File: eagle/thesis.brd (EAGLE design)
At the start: 99.1 x 60.2 mm, 18 parts, among them J1 RJ11-6PTH, U1 ITG-3200, U2 ADXL362

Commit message: wrote a bunch and added references and pictures
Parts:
- renumbered J1 to JHMR2300, U$4 to HMC5883L
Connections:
- net 33V: now also C6.2
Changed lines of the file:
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@@
 <attribute name="PROD_ID" value="IC-11297" x="92.964" y="5.842" size="1.778" layer="27" display="off"/>
 </element>
-<element name="J1" library="SparkFun-Connectors" package="RJ11-6" value="RJ11-6PTH" x="12.319" y="51.181" rot="R180"/>
-<element name="U$4" library="HMC5883L_Breakout-v11" package="SPARKFUN_16LPCC" value="SPARKFUN_HMC5883LSMD" x="60.071" y="43.815" smashed="yes" rot="R90">
+<element name="JHMR2300" library="SparkFun-Connectors" package="RJ11-6" value="RJ11-6PTH" x="12.319" y="51.181" rot="R180"/>
+<element name="HMC5883L" library="HMC5883L_Breakout-v11" package="SPARKFUN_16LPCC" value="SPARKFUN_HMC5883LSMD" x="60.071" y="43.815" smashed="yes" rot="R90">
 <attribute name="VALUE" x="62.611" y="41.91" size="0.6096" layer="27" rot="R90"/>
 </element>
@@
 <signal name="N$5">
 <contactref element="C5" pad="1"/>
-<contactref element="U$4" pad="8"/>
+<contactref element="HMC5883L" pad="8"/>
 <wire x1="62.992" y1="44.577" x2="61.468" y2="44.577" width="0.254" layer="1"/>
 <wire x1="62.992" y1="46.736" x2="62.992" y2="44.577" width="0.254" layer="1"/>
@@
 </signal>
 <signal name="N$7">
-<contactref element="U$4" pad="12"/>
+<contactref element="HMC5883L" pad="12"/>
 <contactref element="C5" pad="2"/>
 <wire x1="58.166" y1="46.355" x2="59.309" y2="45.212" width="0.254" layer="1"/>
@@
 </signal>
 <signal name="N$12">
-<contactref element="U$4" pad="10"/>
+<contactref element="HMC5883L" pad="10"/>
 <contactref element="C3" pad="1"/>
 <wire x1="60.325" y1="44.069" x2="60.325" y2="45.085" width="0.254" layer="1"/>
@@
 <contactref element="U2" pad="P$14"/>
 <contactref element="U$1" pad="3V3"/>
-<contactref element="U$4" pad="2"/>
-<contactref element="U$4" pad="4"/>
-<contactref element="U$4" pad="13"/>
-<contactref element="R2" pad="2"/>
-<contactref element="R1" pad="2"/>
 <contactref element="C4" pad="1"/>
 <contactref element="U1" pad="9"/>
-<contactref element="J1" pad="2"/>
+<contactref element="JHMR2300" pad="2"/>
 <wire x1="41.402" y1="45.466" x2="41.402" y2="45.085" width="0.254" layer="1"/>
 <wire x1="41.402" y1="45.085" x2="41.307" y2="45.081" width="0.254" layer="1"/>
@@
 <wire x1="40.513" y1="46.99" x2="40.513" y2="45.593" width="0.254" layer="1"/>
 <wire x1="41.148" y1="47.625" x2="40.513" y2="46.99" width="0.254" layer="1"/>
-<wire x1="57.023" y1="46.228" x2="58.3565" y2="44.8945" width="0.254" layer="1"/>
-<wire x1="58.3565" y1="44.8945" x2="58.674" y2="44.577" width="0.254" layer="1"/>
-<wire x1="57.023" y1="46.482" x2="57.023" y2="46.228" width="0.254" layer="1"/>
-<wire x1="56.134" y1="47.371" x2="57.023" y2="46.482" width="0.254" layer="1"/>
-<wire x1="58.674" y1="44.577" x2="58.701" y2="44.565" width="0.254" layer="1"/>
-<wire x1="56.134" y1="47.371" x2="56.134" y2="47.459" width="0.254" layer="1"/>
-<wire x1="59.817" y1="41.148" x2="59.817" y2="42.418" width="0.254" layer="1"/>
-<wire x1="60.706" y1="39.624" x2="59.817" y2="41.148" width="0.254" layer="1"/>
-<wire x1="59.817" y1="42.418" x2="59.821" y2="42.445" width="0.254" layer="1"/>
-<wire x1="60.706" y1="39.624" x2="60.794" y2="39.624" width="0.254" layer="1"/>
 <wire x1="60.833" y1="39.624" x2="60.833" y2="41.275" width="0.254" layer="1"/>
 <wire x1="60.833" y1="41.275" x2="60.833" y2="42.418" width="0.254" layer="1"/>
-<wire x1="60.833" y1="42.418" x2="60.821" y2="42.445" width="0.254" layer="1"/>
-<wire x1="60.833" y1="39.624" x2="60.794" y2="39.624" width="0.254" layer="1"/>
 <wire x1="60.833" y1="41.275" x2="63.881" y2="44.323" width="0.254" layer="1"/>
 <wire x1="63.881" y1="44.323" x2="63.881" y2="44.436" width="0.254" layer="1"/>
@@
 <wire x1="63.881" y1="44.436" x2="63.881" y2="44.958" width="0.254" layer="1"/>
 <wire x1="78.105" y1="49.784" x2="78.105" y2="49.856" width="0.254" layer="1"/>
-<wire x1="56.388" y1="43.18" x2="58.3565" y2="44.8945" width="0.254" layer="1"/>
-<wire x1="56.388" y1="41.148" x2="56.388" y2="43.18" width="0.254" layer="1"/>
-<wire x1="59.817" y1="41.148" x2="56.388" y2="41.148" width="0.254" layer="1"/>
 <wire x1="60.452" y1="45.466" x2="41.148" y2="45.466" width="0.254" layer="16"/>
 <wire x1="61.341" y1="46.355" x2="60.452" y2="45.466" width="0.254" layer="16"/>
@@
 <contactref element="C7" pad="2"/>
 <contactref element="U1" pad="13"/>
-<wire x1="42.037" y1="48.895" x2="42.051" y2="48.895" width="0" layer="19" extent="1-1"/>
+<contactref element="R2" pad="2"/>
+<contactref element="R1" pad="2"/>
+<wire x1="57.023" y1="46.228" x2="58.3565" y2="44.8945" width="0.254" layer="1"/>
+<wire x1="58.3565" y1="44.8945" x2="58.674" y2="44.577" width="0.254" layer="1"/>
+<wire x1="57.023" y1="46.482" x2="57.023" y2="46.228" width="0.254" layer="1"/>
+<wire x1="56.134" y1="47.371" x2="57.023" y2="46.482" width="0.254" layer="1"/>
+<wire x1="59.817" y1="41.148" x2="59.817" y2="42.418" width="0.254" layer="1"/>
+<wire x1="60.706" y1="39.624" x2="59.817" y2="41.148" width="0.254" layer="1"/>
+<wire x1="60.706" y1="39.624" x2="60.794" y2="39.624" width="0.254" layer="1"/>
+<wire x1="56.388" y1="43.18" x2="58.3565" y2="44.8945" width="0.254" layer="1"/>
+<wire x1="56.388" y1="41.148" x2="56.388" y2="43.18" width="0.254" layer="1"/>
+<wire x1="59.817" y1="41.148" x2="56.388" y2="41.148" width="0.254" layer="1"/>
+<contactref element="HMC5883L" pad="2"/>
+<contactref element="HMC5883L" pad="4"/>
+<contactref element="HMC5883L" pad="13"/>
+<contactref element="C6" pad="2"/>
+<wire x1="56.134" y1="47.371" x2="56.134" y2="47.459" width="0" layer="19" extent="1-1"/>
+<wire x1="58.701" y1="44.565" x2="58.674" y2="44.577" width="0" layer="19" extent="1-1"/>
+<wire x1="59.821" y1="42.445" x2="59.817" y2="42.418" width="0" layer="19" extent="1-1"/>
+<wire x1="60.833" y1="39.624" x2="60.794" y2="39.624" width="0" layer="19" extent="1-1"/>
+<wire x1="42.051" y1="48.895" x2="42.037" y2="48.895" width="0" layer="19" extent="1-1"/>
+<wire x1="60.821" y1="42.445" x2="60.833" y2="42.418" width="0" layer="19" extent="1-1"/>
 <wire x1="41.307" y1="45.581" x2="41.275" y2="45.593" width="0" layer="19" extent="1-1"/>
 <wire x1="42.057" y1="42.831" x2="42.037" y2="42.799" width="0" layer="19" extent="1-1"/>
 <wire x1="41.402" y1="45.466" x2="41.307" y2="45.581" width="0" layer="19" extent="1-1"/>
+<wire x1="42.559" y1="40.259" x2="42.037" y2="42.799" width="0" layer="19" extent="1-1"/>
 </signal>
 <signal name="5V">
@@
 <signal name="VIN">
 <contactref element="U$1" pad="VIN"/>
-<contactref element="J1" pad="5"/>
+<contactref element="JHMR2300" pad="5"/>
 <wire x1="40.259" y1="8.255" x2="42.926" y2="5.588" width="0.254" layer="16"/>
 <wire x1="19.558" y1="8.255" x2="40.259" y2="8.255" width="0.254" layer="16"/>
@@
 </signal>
 <signal name="TX1">
-<contactref element="J1" pad="4"/>
+<contactref element="JHMR2300" pad="4"/>
 <contactref element="U$1" pad="TX1"/>
 <wire x1="74.041" y1="55.753" x2="75.946" y2="53.848" width="0.254" layer="16"/>
@@
 </signal>
 <signal name="RX1">
-<contactref element="J1" pad="3"/>
+<contactref element="JHMR2300" pad="3"/>
 <contactref element="U$1" pad="RX1"/>
 <wire x1="75.184" y1="50.546" x2="78.486" y2="53.848" width="0.254" layer="16"/>
@@
 <signal name="SCL">
 <contactref element="U$3" pad="7"/>
-<contactref element="U$4" pad="1"/>
+<contactref element="HMC5883L" pad="1"/>
 <contactref element="R2" pad="1"/>
 <contactref element="U$1" pad="SCL"/>
@@
 </signal>
 <signal name="SDA" airwireshidden="yes">
-<contactref element="U$4" pad="16"/>
+<contactref element="HMC5883L" pad="16"/>
 <contactref element="R1" pad="1"/>
 <contactref element="U$1" pad="SDA"/>
@@
 <signal name="GND1_1">
 <contactref element="U$1" pad="GND1"/>
-<contactref element="J1" pad="1"/>
+<contactref element="JHMR2300" pad="1"/>
 <contactref element="U$6" pad="GND"/>
 <contactref element="U$2" pad="6"/>
@@
 <contactref element="C3" pad="2"/>
 <contactref element="C4" pad="2"/>
-<contactref element="U$4" pad="9"/>
-<contactref element="U$4" pad="11"/>
+<contactref element="HMC5883L" pad="9"/>
+<contactref element="HMC5883L" pad="11"/>
 <wire x1="44.577" y1="40.513" x2="44.577" y2="41.783" width="0.254" layer="1"/>
 <wire x1="44.577" y1="41.783" x2="44.577" y2="42.799" width="0.254" layer="1"/>

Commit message: wrote more.
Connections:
- new net SCL1: U$1.SCL1, U1.23
- new net SDA1: U$1.SDA1, U1.24
- net 33V: now also JHMR2300.5; no longer JHMR2300.2
- net GND1_1: now also JHMR2300.6; no longer JHMR2300.1
- net RX1: now also JHMR2300.4; no longer JHMR2300.3
- net SCL: no longer U1.23
- net SDA: no longer U1.24
- net TX1: now also JHMR2300.3; no longer JHMR2300.4
- net VIN: now also JHMR2300.2; no longer JHMR2300.5
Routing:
- net SCL1: track 0.00 -> 41.9 mm
- net SDA1: track 0.00 -> 36.0 mm
- net D48: track 123.3 -> 102.7 mm, vias 0 -> 1
- net SDA: track 88.6 -> 104.8 mm
- net D47: track 103.1 -> 117.7 mm, vias 2 -> 1
- net RX3: track 87.1 -> 100.8 mm
- net TX3: track 76.0 -> 88.9 mm
- net SCLK: track 128.9 -> 117.7 mm
- net RX1: track 77.3 -> 87.5 mm
- net D38: track 79.5 -> 71.3 mm
- net D41: track 79.4 -> 71.5 mm, vias 0 -> 1
- net GNDHEAD: track 97.5 -> 90.0 mm, vias 0 -> 3
- net 5V: track 52.9 -> 59.4 mm
- net D49: track 100.5 -> 105.3 mm, vias 2 -> 0
- net 33V: track 232.8 -> 237.1 mm
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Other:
- board text added: "ADAM CHASE 09/10/13 FDR v2.10"
- board text removed: "ADAM CHASE 08/13/13 FDR v2.00"

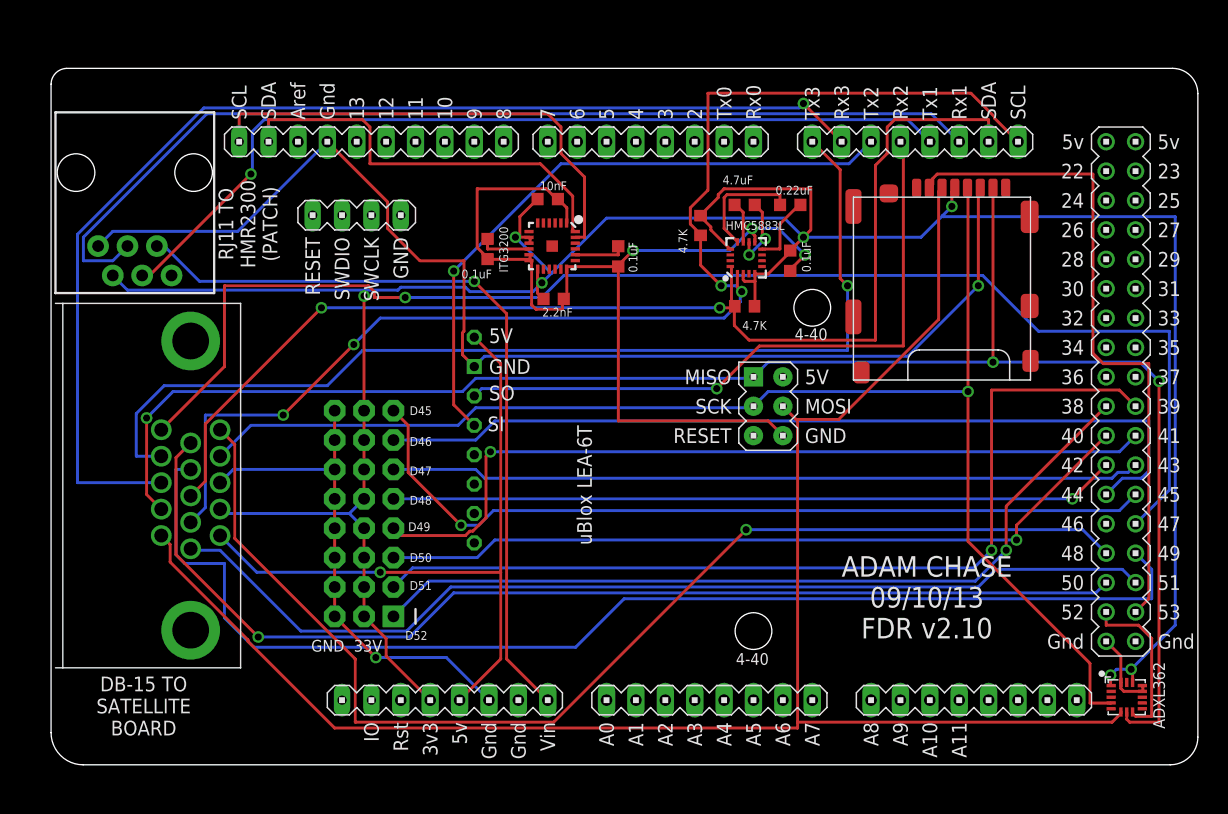
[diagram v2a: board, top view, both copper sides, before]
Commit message: added breakout board libraries and changed thesis.brd
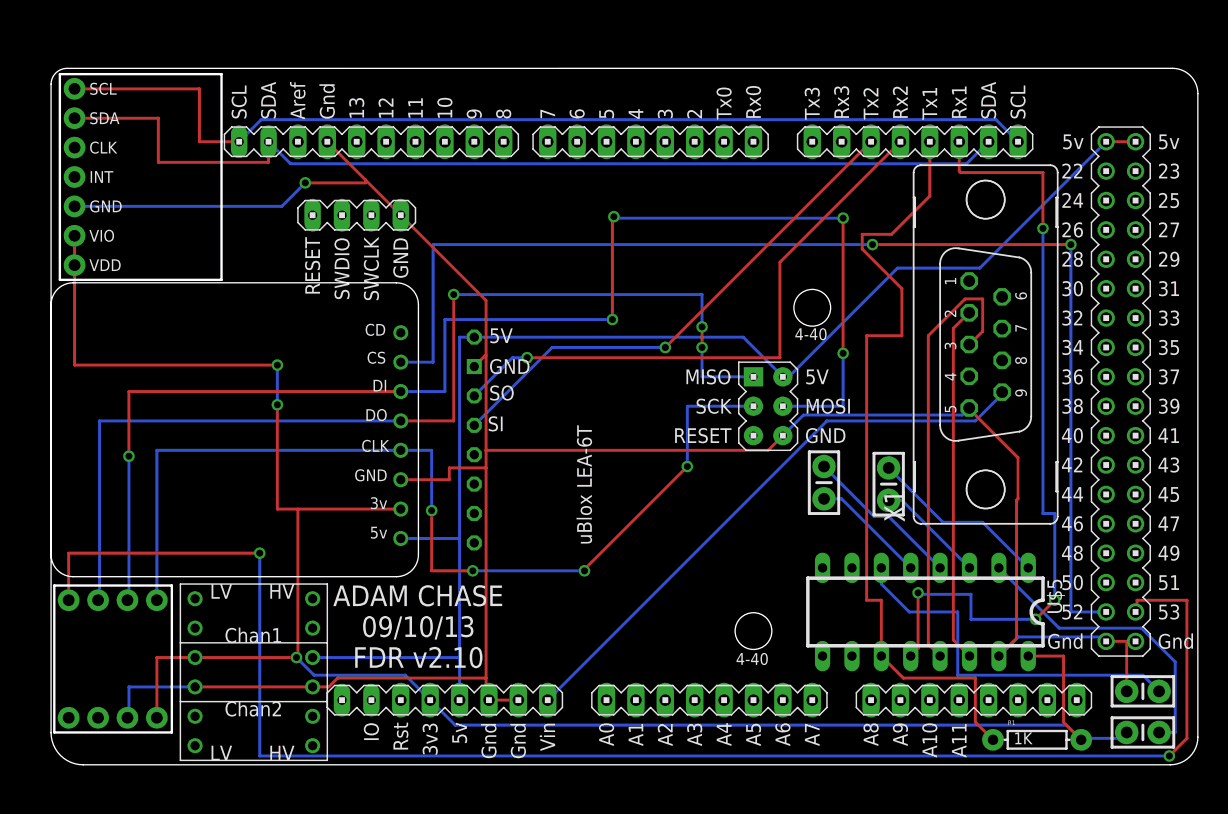
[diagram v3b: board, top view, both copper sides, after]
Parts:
- removed C5: 0.22uF, rcl:C0603K
- removed C6: 0.1uF, rcl:C0603K
- removed C7: 10nF, rcl:C0603K
- removed HMC5883L: SPARKFUN_HMC5883LSMD, HMC5883L_Breakout-v11:SPARKFUN_16LPCC
- removed JHMR2300: RJ11-6PTH, SparkFun-Connectors:RJ11-6
- removed R2: 4.7K, rcl:R0603
- removed U1: ITG-3200, SparkFun:QFN-24
- removed U2: ADXL362, SparkFun-Sensors:ADXL362
- added U$4: ADXL362, adxl362:ADXL362
- added U$7: ITG3200, ITG3200:ITG3200
- added X1: (no value), con-subd:F09V
- C1, C4: value 0.1uF -> 100nF; device rcl:C0603K -> SparkFun-Passives:CAP-PTH-SMALL-KIT
- C2: value 2.2nF -> 100nF; device rcl:C0603K -> SparkFun-Passives:CAP-PTH-SMALL-KIT
- C3: value 4.7uF -> 100nF; device rcl:C0603K -> SparkFun-Passives:CAP-PTH-SMALL-KIT
- R1: value 4.7K -> 1K; device rcl:R0603 -> SparkFun-Resistors:AXIAL-0.3
- U$2: value MICROSD_SPI_MODE -> LOGIC_LEVEL_CONVERTER; device con-molex-microsd:MICRO_SD_CONNECTOR -> SparkFun-Boards:LOGIC_LEVEL_CONVERTER
- U$3: value VGA-F90S -> MICROSD; device VideoConnectors:DB-15-F90+SHIELD-SMALL_PADS -> MICROSD:MICROSD
- U$5: value HEADER-3X8SERVO -> ICL3232; device pixhawk2:3X8RA -> SparkFun-DigitalIC:DIL16
- moved U$2 77.6 mm to (11.2, 0.38)
- moved C3 54.3 mm to (94.4, 6.35)
- moved C4 50.9 mm to (94.4, 2.79), turned to 0 degrees
- moved U$5 48.0 mm to (75.6, 13.2)
- moved R1 45.2 mm to (85.2, 2.16)
- moved C1 40.2 mm to (72.4, 24.3), turned to 270 degrees
- moved C2 26.4 mm to (66.8, 24.4), turned to 270 degrees
- moved U$3 8.41 mm to (-0.25, 15.7), turned to 0 degrees
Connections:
- removed net 33V: C4.1, C6.2, C7.2, HMC5883L.13, HMC5883L.2, HMC5883L.4, JHMR2300.5, R1.2, R2.2, U$1.3V3, U$2.4, U$3.2, U$5.11, U$5.14, U$5.17, U$5.2, U$5.20, U$5.23, U$5.5, U$5.8, U1.13, U1.8, U1.9, U2.P$1, U2.P$14
- removed net CPOUT: C2.2, U1.20
- removed net D52: U$1.52, U2.P$8
- removed net D53: U$1.53, U$2.2
- removed net GND1: U$1.GND_1, U$3.3, U$5.12, U$5.15, U$5.18, U$5.21, U$5.24, U$5.3, U$5.6, U$5.9
- removed net GND1_1: JHMR2300.6, U$1.GND1, U$2.6, U$6.GND
- removed net GND2: U$1.GND_2
- removed net GNDA: U$1.GND_A, U2.P$12, U2.P$13, U2.P$16
- removed net GNDHEAD: C1.1, C2.1, C3.2, C4.2, C6.1, C7.1, HMC5883L.11, HMC5883L.9, U$1.5V_ICSP, U1.1, U1.11, U1.12, U1.18
- removed net N$12: C3.1, HMC5883L.10
- removed net N$14: C1.2, U1.10
- removed net N$5: C5.1, HMC5883L.8
- removed net N$7: C5.2, HMC5883L.12
- removed net RX1: JHMR2300.4, U$1.RX1
- removed net SCL1: U$1.SCL1, U1.23
- removed net SDA: HMC5883L.16, R1.1, U$1.SDA, U$3.8
- removed net SDA1: U$1.SDA1, U1.24
- removed net TX1: JHMR2300.3, U$1.TX1
- new net 3V3: C4.1, R1.P$2, U$1.3V3, U$2.P$3, U$3.3V, U$4.VCC, U$5.16, U$7.VDD, U$7.VIO
- new net ACCELCS: U$1.53, U$4.CS
- new net C1+: C1.1, U$5.1
- new net C1-: C1.2, U$5.3
- new net C2+: C2.1, U$5.4
- new net C2-: C2.2, U$5.5
- new net GND: C3.2, U$1.5V_ICSP, U$1.GND1, U$1.GND_1, U$1.GND_2, U$1.GND_A, U$1.GND_B, U$1.GND_DEBUG, U$2.P$4, U$2.P$9, U$3.GND, U$4.GND, U$5.15, U$6.GND, U$7.GND, X1.5
- new net MAGSI: R1.P$1, U$1.TX1, U$5.11
- new net MAGSO: U$1.RX1, U$5.12
- new net RS232SI: U$5.13, X1.3
- new net RS232SO: U$5.14, X1.2
- new net SDA2: U$1.SDA, U$1.SDA1, U$7.SDA
- new net SDCS: U$1.52, U$3.CS
- new net V+: C4.2, U$5.2
- new net V-: C3.1, U$5.6
- net 5V: now also U$1.5V_A, U$1.5V_B, U$1.GND_ICSP, U$2.P$10, U$3.5V; no longer U$3.1
- net D38: no longer U$5.1
- net D39: no longer U$5.4
- net D40: no longer U$5.7
- net D41: no longer U$5.10
- net D42: no longer U$5.13
- net D43: no longer U$5.16
- net D44: no longer U$5.19
- net D45: no longer U$5.22
- net D47: no longer U$3.15
- net D48: no longer U$3.5
- net D49: no longer U$3.9
- net D50: no longer U$3.10
- net D51: no longer U$3.6
- net MISO: now also U$3.DO, U$4.MISO; no longer U$2.7, U$3.12, U2.P$7
- net MOSI: now also U$3.DI, U$4.MOSI; no longer U$2.3, U$3.11, U2.P$6
- net RX3: no longer U$3.13
- net SCL: now also U$1.SCL1, U$7.SCL; no longer HMC5883L.1, R2.1, U$3.7
- net SCLK: now also U$3.CLK, U$4.SCK; no longer U$2.5, U$3.4, U2.P$4
- net TX3: no longer U$3.14
- net VIN: now also X1.9; no longer JHMR2300.2
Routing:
- net 33V: track 237.1 -> 0.00 mm, vias 7 -> 0
- net GND: track 0.00 -> 210.7 mm, vias 0 -> 1
- net 3V3: track 0.00 -> 168.0 mm, vias 0 -> 3
- net ACCELCS: track 0.00 -> 136.3 mm, vias 0 -> 2
- net D47: track 117.7 -> 0.00 mm, vias 1 -> 0
- net GND1_1: track 105.5 -> 0.00 mm, vias 1 -> 0
- net D49: track 105.3 -> 0.00 mm
- net SDA: track 104.8 -> 0.00 mm, vias 2 -> 0
- net SDCS: track 0.00 -> 102.9 mm, vias 0 -> 2
- net D48: track 102.7 -> 0.00 mm, vias 1 -> 0
- net RX3: track 100.8 -> 0.00 mm, vias 1 -> 0
- net D50: track 95.5 -> 0.00 mm, vias 1 -> 0
- net GNDHEAD: track 90.0 -> 0.00 mm, vias 3 -> 0
- net TX3: track 88.9 -> 0.00 mm, vias 1 -> 0
- net RX1: track 87.5 -> 0.00 mm
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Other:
- board text removed: "0.1uF"
- board text removed: "0.22uF"
- board text removed: "10nF"
- board text removed: "2.2nF"
- board text removed: "33V"
- board text removed: "4.7K"
- board text removed: "4.7uF"
- board text removed: "ADXL362"
- board text removed: "D45"
- board text removed: "D46"
- board text removed: "D47"
- board text removed: "D48"
- board text removed: "D49"
- board text removed: "D50"
- board text removed: "D51"
- board text removed: "D52"
- board text removed: "DB-15 TO SATELLITE BOARD"
- board text removed: "HMC5883L"
- board text removed: "ITG3200"
- board text removed: "RJ11 TO HMR2300 (PATCH)"

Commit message: added smaller satellite board
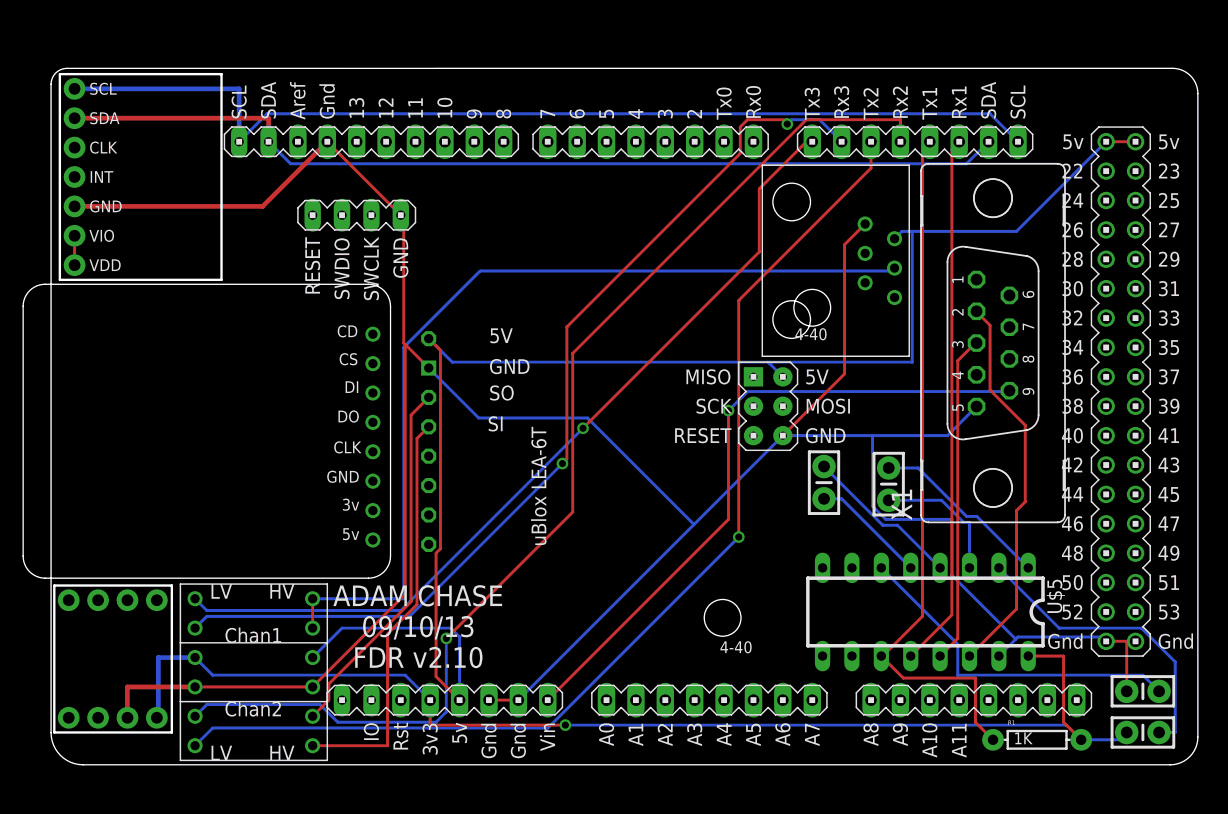
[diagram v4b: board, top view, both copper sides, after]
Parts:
- added U$8: RJ11V, RJ11V:RJ11V
- moved U$6 3.94 mm to (30.1, 50.8)
- moved U$3 2.42 mm to (-2.67, 15.6)
- moved X1 0.65 mm to (81.4, 36.4)
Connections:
- new net RX2H: U$2.P$8, U$6.TTLDO
- new net RX3H: U$8.P$5
- new net TX2H: U$2.P$7, U$6.TTLDI
- new net TX3H: U$2.P$11, U$2.P$12, U$8.P$2
- net 5V: now also U$8.P$3
- net GND: now also U$8.P$6
- net RX2: now also U$2.P$5; no longer U$6.TTLDO
- net RX3: now also U$2.P$2
- net TX2: now also U$2.P$6; no longer U$6.TTLDI
- net TX3: now also U$2.P$1
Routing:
- net ACCELCS: track 136.3 -> 0.00 mm, vias 2 -> 0
- net MOSI: track 116.6 -> 0.00 mm, vias 5 -> 0
- net SDCS: track 102.9 -> 0.00 mm, vias 2 -> 0
- net MISO: track 90.2 -> 0.00 mm, vias 3 -> 0
- net SCLK: track 84.1 -> 0.00 mm, vias 4 -> 0
- net RX3: track 0.00 -> 83.4 mm, vias 0 -> 2
- net TX3H: track 0.00 -> 77.4 mm
- net TX3: track 0.00 -> 73.7 mm, vias 0 -> 1
- net 3V3: track 168.0 -> 107.0 mm, vias 3 -> 1
- net TX2: track 44.4 -> 93.4 mm
- net RX2: track 50.8 -> 97.2 mm
- net TX2H: track 0.00 -> 35.5 mm
- net GND: track 210.7 -> 244.3 mm, vias 1 -> 0
- net RX2H: track 0.00 -> 31.7 mm
- net MAGSO: track 68.2 -> 46.2 mm, vias 4 -> 0
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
